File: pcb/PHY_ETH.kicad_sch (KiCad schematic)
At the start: 15 parts, among them U1 LAN8742A, Y1 LFXTAL071758Cutt

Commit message: updated ethernet
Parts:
- added C39: 470pF, Capacitor_SMD:C_0603_1608Metric_Pad1.08x0.95mm_HandSolder, symbol Device:C
- added C40: 1uF, Capacitor_SMD:C_0603_1608Metric_Pad1.08x0.95mm_HandSolder, symbol Device:C
- added C57: 1u, Capacitor_SMD:C_0603_1608Metric, symbol Device:C
- added C58: 1nF, Capacitor_SMD:C_0603_1608Metric_Pad1.08x0.95mm_HandSolder, symbol Device:C
- added C63: 100nF, Capacitor_SMD:C_0603_1608Metric_Pad1.08x0.95mm_HandSolder, symbol Device:C
- added D9: ESDA6V1SC5, Package_TO_SOT_SMD:SOT-23-5, symbol Power_Protection:ESDA6V1SC5
- added FB2: FCM 1608KF-471T03, Inductor_SMD:L_0603_1608Metric_Pad1.05x0.95mm_HandSolder, symbol Device:FerriteBead
- added R27, R28, R41: 10k, Resistor_SMD:R_0603_1608Metric_Pad0.98x0.95mm_HandSolder, symbol Device:R
- added R42, R44, R45: 49.9R, Resistor_SMD:R_0603_1608Metric_Pad0.98x0.95mm_HandSolder, symbol Device:R
- added R50, R51: 75R, Resistor_SMD:R_0603_1608Metric_Pad0.98x0.95mm_HandSolder, symbol Device:R
- added TR1: PT61017PEL, Transformer_SMD:Transformer_Ethernet_Bourns_PT61017PEL, symbol Transformer:PT61017PEL
- C3: value 10uF -> 100nF
- C5, C6: value 10pF -> 8pF
- R10: value 12.4k -> 12.1k
- R8: value 10R -> 49.9R
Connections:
- net 3V3: now also C57.1, FB2.2, R27.1, R28.1, R41.1; no longer R8.1, U1.6 (VDDCR)
- net ETH_CRS_DV: now also R41.2
- net ETH_RXD0: now also R27.2
- net ETH_RXD1: now also R28.2
- net ETH_RXM: now also D9.5 (K), R51.1, TR1.10 (C_RX), TR1.9 (RX-); no longer U1.22 (RXN)
- net ETH_RXP: now also D9.4 (K), TR1.11 (RX+); no longer U1.23 (RXP)
- net ETH_TXM: now also D9.3 (K), TR1.14 (TX-); no longer U1.20 (TXN)
- net ETH_TXP: now also D9.1 (K), TR1.16 (TX+); no longer U1.21 (TXP)
- net GND: now also R9.2, C39.2, C40.2, C57.2, C58.2, C63.2, D9.2 (A); no longer D4.1 (K)
- net at D3.1 (K), R7.2: now also D3.2 (A), U1.2 (LED2/~{INTSEL})
- net at D4.2 (A): now also U1.3 (LED1/REGOFF); no longer R9.2
- net at R9.1: now also D4.1 (K); no longer U1.3 (LED1/REGOFF)
- net at C2.1, C3.1, U1.1 (VDD2A)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: now also R8.1, C63.1, FB2.1, R42.1, R44.1, R45.1, TR1.2 (C_TD), TR1.7 (C_RD); no longer R8.2
- new net: C58.1, R50.2, R51.2
- new net: R42.2, TR1.3 (TD-), U1.20 (TXN)
- new net: R8.2, TR1.1 (TD+), U1.21 (TXP)
- new net: R45.2, TR1.8 (RD-), U1.22 (RXN)
- new net: R44.2, TR1.6 (RD+), U1.23 (RXP)
- new net: C39.1, C40.1, U1.6 (VDDCR)
- new net: R50.1, TR1.15 (C_TX)
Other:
- moved on the sheet: C2, C3, C4, C5, C6, D3, D4, R10, R11, R12, R7, R9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

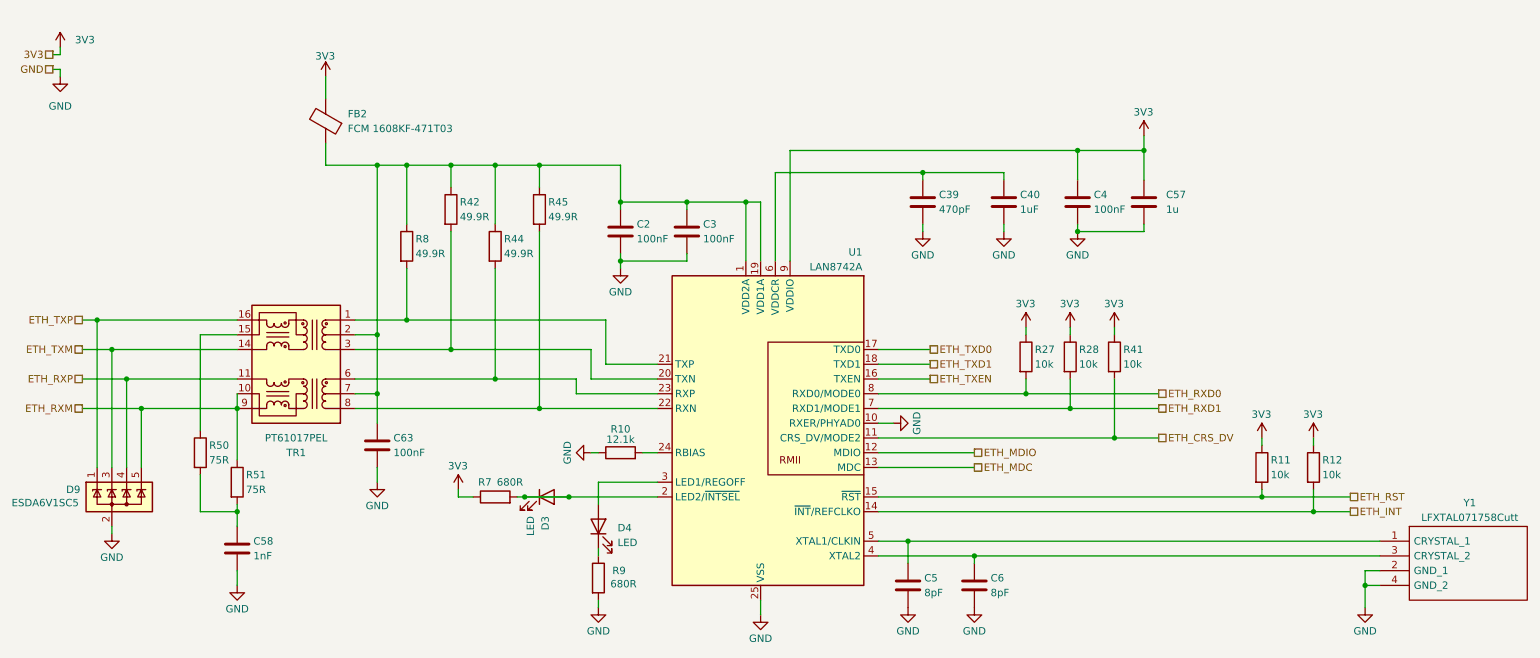
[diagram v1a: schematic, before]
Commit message: reannotated, updated some symbols
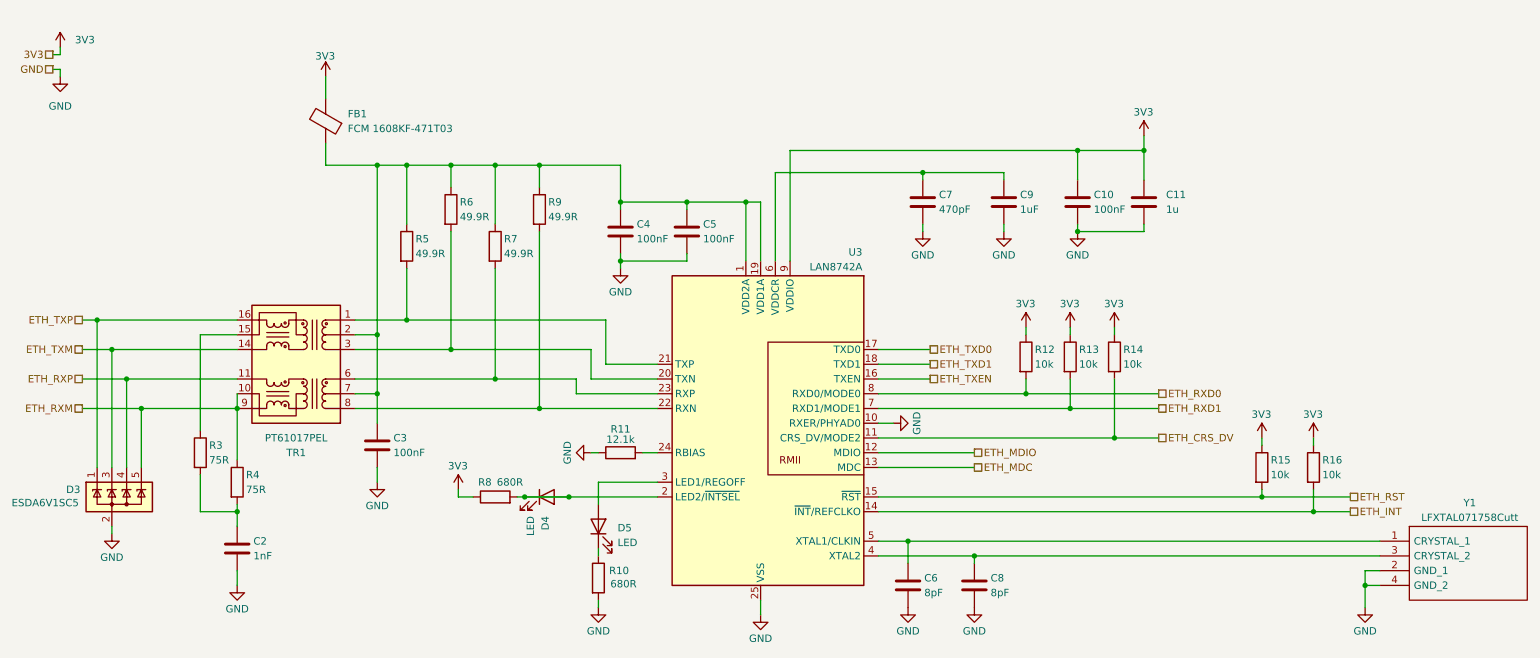
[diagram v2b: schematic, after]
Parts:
- renumbered C4 to C10, C57 to C11, C58 to C2, C63 to C3, C2 to C4, C3 to C5, C5 to C6, C39 to C7, C6 to C8, C40 to C9, D9 to D3, D3 to D4, D4 to D5, FB2 to FB1, R9 to R10, R10 to R11, R27 to R12, R28 to R13, R41 to R14, R11 to R15, R12 to R16, R50 to R3, R51 to R4, R8 to R5, R42 to R6, R44 to R7, R7 to R8, R45 to R9, U1 to U3

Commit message: minor changes before layout
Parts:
- added TP20: ETH_RST, TestPoint:TestPoint_THTPad_D2.0mm_Drill1.0mm, symbol Connector:TestPoint
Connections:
- net ETH_INT: now also R15.2; no longer R16.2
- net ETH_RST: now also R16.2, TP20.1; no longer R15.2
- net at D4.1 (K), R8.2: no longer D4.2 (A), U3.2 (LED2/~{INTSEL})
- new net: D4.2 (A), U3.2 (LED2/~{INTSEL})
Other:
- moved on the sheet: R15, R16
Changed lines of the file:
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@@
 	(paper "A4")
 	(junction
-		(at 114.3 101.6)
-		(diameter 0)
-		(color 0 0 0 0)
-	)
-	(junction
-		(at 233.68 101.6)
+		(at 232.41 104.14)
 		(diameter 0)
 		(color 0 0 0 0)
@@
 	)
 	(junction
-		(at 101.6 44.45)
+		(at 241.3 101.6)
 		(diameter 0)
 		(color 0 0 0 0)
 	)
 	(junction
-		(at 144.78 50.8)
+		(at 101.6 44.45)
 		(diameter 0)
 		(color 0 0 0 0)
 	)
 	(junction
-		(at 106.68 101.6)
+		(at 144.78 50.8)
 		(diameter 0)
 		(color 0 0 0 0)
@@
 	)
 	(junction
-		(at 242.57 104.14)
+		(at 184.15 111.76)
 		(diameter 0)
 		(color 0 0 0 0)
 	)
 	(junction
-		(at 184.15 111.76)
+		(at 57.15 104.14)
 		(diameter 0)
 		(color 0 0 0 0)
 	)
 	(junction
-		(at 57.15 104.14)
+		(at 241.3 90.17)
 		(diameter 0)
 		(color 0 0 0 0)
@@
 	(wire
 		(pts
-			(xy 114.3 101.6) (xy 106.68 101.6)
-		)
-		(stroke
-			(width 0)
-			(type default)
-		)
-	)
-	(wire
-		(pts
 			(xy 184.15 93.98) (xy 167.64 93.98)
 		)
@@
 	(wire
 		(pts
-			(xy 242.57 91.44) (xy 242.57 92.71)
+			(xy 241.3 71.12) (xy 241.3 72.39)
 		)
 		(stroke
@@
 	(wire
 		(pts
-			(xy 167.64 104.14) (xy 242.57 104.14)
+			(xy 167.64 104.14) (xy 232.41 104.14)
 		)
 		(stroke
@@
 	(wire
 		(pts
-			(xy 242.57 104.14) (xy 248.92 104.14)
+			(xy 149.86 45.72) (xy 175.26 45.72)
 		)
 		(stroke
@@
 	(wire
 		(pts
-			(xy 149.86 45.72) (xy 175.26 45.72)
+			(xy 241.3 101.6) (xy 248.92 101.6)
 		)
 		(stroke
@@
 	(wire
 		(pts
-			(xy 233.68 100.33) (xy 233.68 101.6)
-		)
-		(stroke
-			(width 0)
-			(type default)
-		)
-	)
-	(wire
-		(pts
 			(xy 109.22 44.45) (xy 109.22 48.26)
 		)
@@
 	(wire
 		(pts
-			(xy 233.68 101.6) (xy 248.92 101.6)
-		)
-		(stroke
-			(width 0)
-			(type default)
-		)
-	)
-	(wire
-		(pts
 			(xy 95.25 100.33) (xy 95.25 101.6)
 		)
@@
 	(wire
 		(pts
+			(xy 241.3 90.17) (xy 241.3 101.6)
+		)
+		(stroke
+			(width 0)
+			(type default)
+		)
+	)
+	(wire
+		(pts
+			(xy 241.3 90.17) (xy 242.57 90.17)
+		)
+		(stroke
+			(width 0)
+			(type default)
+		)
+	)
+	(wire
+		(pts
 			(xy 213.36 55.88) (xy 213.36 54.61)
 		)
@@
 	(wire
 		(pts
-			(xy 233.68 91.44) (xy 233.68 92.71)
+			(xy 232.41 71.12) (xy 232.41 85.09)
 		)
 		(stroke
@@
 	(wire
 		(pts
-			(xy 167.64 101.6) (xy 233.68 101.6)
+			(xy 167.64 101.6) (xy 241.3 101.6)
 		)
 		(stroke
@@
 	(wire
 		(pts
+			(xy 232.41 92.71) (xy 232.41 104.14)
+		)
+		(stroke
+			(width 0)
+			(type default)
+		)
+	)
+	(wire
+		(pts
 			(xy 175.26 45.72) (xy 189.23 45.72)
 		)
@@
 	(wire
 		(pts
+			(xy 241.3 80.01) (xy 241.3 90.17)
+		)
+		(stroke
+			(width 0)
+			(type default)
+		)
+	)
+	(wire
+		(pts
 			(xy 118.11 81.28) (xy 129.54 81.28)
 		)
@@
 	(wire
 		(pts
-			(xy 81.28 73.66) (xy 81.28 44.45)
+			(xy 232.41 104.14) (xy 248.92 104.14)
 		)
 		(stroke
@@
 	(wire
 		(pts
-			(xy 242.57 100.33) (xy 242.57 104.14)
+			(xy 81.28 73.66) (xy 81.28 44.45)
 		)
 		(stroke
@@
 	(symbol
 		(lib_id "Device:R")
-		(at 242.57 96.52 0)
+		(at 241.3 76.2 0)
 		(unit 1)
 		(exclude_from_sim no)
@@
 		(dnp no)
 		(property "Reference" "R16"
-			(at 244.094 95.25 0)
+			(at 242.824 74.93 0)
 			(effects
 				(font
@@
 		)
 		(property "Value" "10k"
-			(at 244.094 97.79 0)
+			(at 242.824 77.47 0)
 			(effects
 				(font
@@
 		)
 		(property "Footprint" "Resistor_SMD:R_0603_1608Metric_Pad0.98x0.95mm_HandSolder"
-			(at 240.792 96.52 90)
+			(at 239.522 76.2 90)
 			(effects
 				(font
@@
 		)
 		(property "Datasheet" "~"
-			(at 242.57 96.52 0)
+			(at 241.3 76.2 0)
 			(effects
 				(font
@@
 		)
 		(property "Description" "Resistor"
-			(at 242.57 96.52 0)
+			(at 241.3 76.2 0)
 			(effects
 				(font
@@
 	)
 	(symbol
+		(lib_id "Connector:TestPoint")
+		(at 242.57 90.17 270)
+		(unit 1)
+		(exclude_from_sim no)
+		(in_bom yes)
+		(on_board yes)
+		(dnp no)
+		(property "Reference" "TP20"
+			(at 243.332 85.852 90)
+			(effects
+				(font
+					(size 1.27 1.27)
+				)
+				(justify left)
+			)
+		)
+		(property "Value" "ETH_RST"
+			(at 243.332 87.884 90)
+			(effects
+				(font
+					(size 1.27 1.27)
+				)
+				(justify left)
+			)
+		)
+		(property "Footprint" "TestPoint:TestPoint_THTPad_D2.0mm_Drill1.0mm"
+			(at 242.57 95.25 0)
+			(effects
+				(font
+					(size 1.27 1.27)
+				)
+				(hide yes)
+			)
+		)
+		(property "Datasheet" "~"
+			(at 242.57 95.25 0)
+			(effects
+				(font
+					(size 1.27 1.27)
+				)
+				(hide yes)
+			)
+		)
+		(property "Description" "test point"
+			(at 242.57 90.17 0)
+			(effects
+				(font
+					(size 1.27 1.27)
+				)
+				(hide yes)
+			)
+		)
+		(pin "1"
+		)
+		(instances
+			(project "NCU"
+				(path "/3aee14c3-5480-4f7c-989e-3fef81779034/9758cbcc-2ab2-405c-935d-3964f8470771"
+					(reference "TP20")
+					(unit 1)
+				)
+			)
+		)
+	)
+	(symbol
 		(lib_id "power:+3V3")
 		(at 193.04 72.39 0)
@@
 	(symbol
 		(lib_id "Device:R")
-		(at 233.68 96.52 0)
+		(at 232.41 88.9 0)
 		(unit 1)
 		(exclude_from_sim no)
@@
 		(dnp no)
 		(property "Reference" "R15"
-			(at 235.204 95.25 0)
+			(at 233.934 87.63 0)
 			(effects
 				(font
@@
 		)
 		(property "Value" "10k"
-			(at 235.204 97.79 0)
+			(at 233.934 90.17 0)
 			(effects
 				(font
@@
 		)
 		(property "Footprint" "Resistor_SMD:R_0603_1608Metric_Pad0.98x0.95mm_HandSolder"
-			(at 231.902 96.52 90)
+			(at 230.632 88.9 90)
 			(effects
 				(font
@@
 		)
 		(property "Datasheet" "~"
-			(at 233.68 96.52 0)
+			(at 232.41 88.9 0)
 			(effects
 				(font
@@
 		)
 		(property "Description" "Resistor"
-			(at 233.68 96.52 0)
+			(at 232.41 88.9 0)
 			(effects
 				(font
@@
 	(symbol
 		(lib_id "power:+3V3")
-		(at 233.68 91.44 0)
+		(at 232.41 71.12 0)
 		(unit 1)
 		(exclude_from_sim no)
@@
 		(dnp no)
 		(property "Reference" "#PWR0114"
-			(at 233.68 95.25 0)
+			(at 232.41 74.93 0)
 			(effects
 				(font
@@
 		)
 		(property "Value" "3V3"
-			(at 231.902 87.376 0)
+			(at 230.632 67.056 0)
 			(effects
 				(font
@@
 		)
 		(property "Footprint" ""
-			(at 233.68 91.44 0)
+			(at 232.41 71.12 0)
 			(effects
 				(font
@@
 		)
 		(property "Datasheet" ""
-			(at 233.68 91.44 0)
+			(at 232.41 71.12 0)
 			(effects
 				(font
@@
 		)
 		(property "Description" "Power symbol creates a global label with name \"+3V3\""
-			(at 233.68 91.44 0)
+			(at 232.41 71.12 0)
 			(effects
 				(font
@@
 	(symbol
 		(lib_id "power:+3V3")
-		(at 242.57 91.44 0)
+		(at 241.3 71.12 0)
 		(unit 1)
 		(exclude_from_sim no)
@@
 		(dnp no)
 		(property "Reference" "#PWR0115"
-			(at 242.57 95.25 0)
+			(at 241.3 74.93 0)
 			(effects
 				(font
@@
 		)
 		(property "Value" "3V3"
-			(at 240.792 87.376 0)
+			(at 239.522 67.056 0)
 			(effects
 				(font
@@
 		)
 		(property "Footprint" ""
-			(at 242.57 91.44 0)
+			(at 241.3 71.12 0)
 			(effects
 				(font
@@
 		)
 		(property "Datasheet" ""
-			(at 242.57 91.44 0)
+			(at 241.3 71.12 0)
 			(effects
 				(font
@@
 		)
 		(property "Description" "Power symbol creates a global label with name \"+3V3\""
-			(at 242.57 91.44 0)
+			(at 241.3 71.12 0)
 			(effects
 				(font

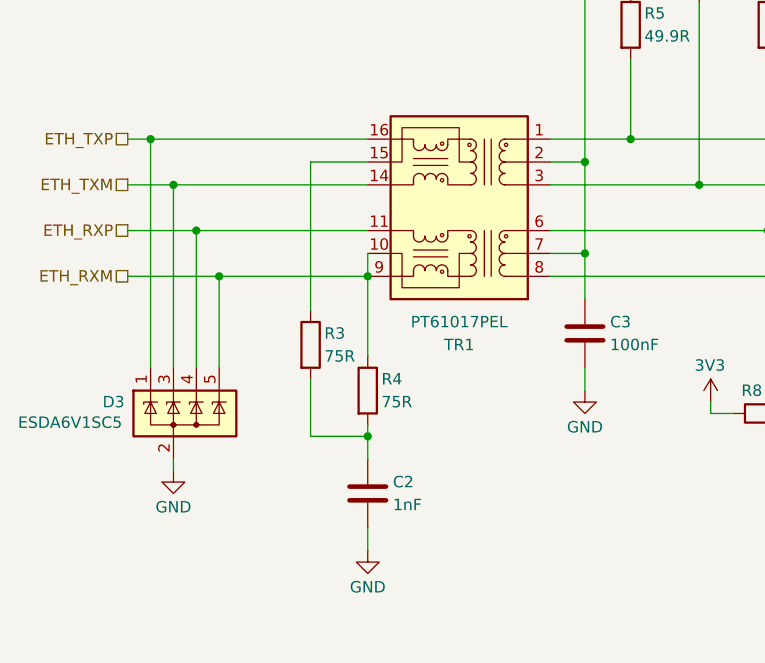
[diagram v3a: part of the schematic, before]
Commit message: first pass of ethernet phy
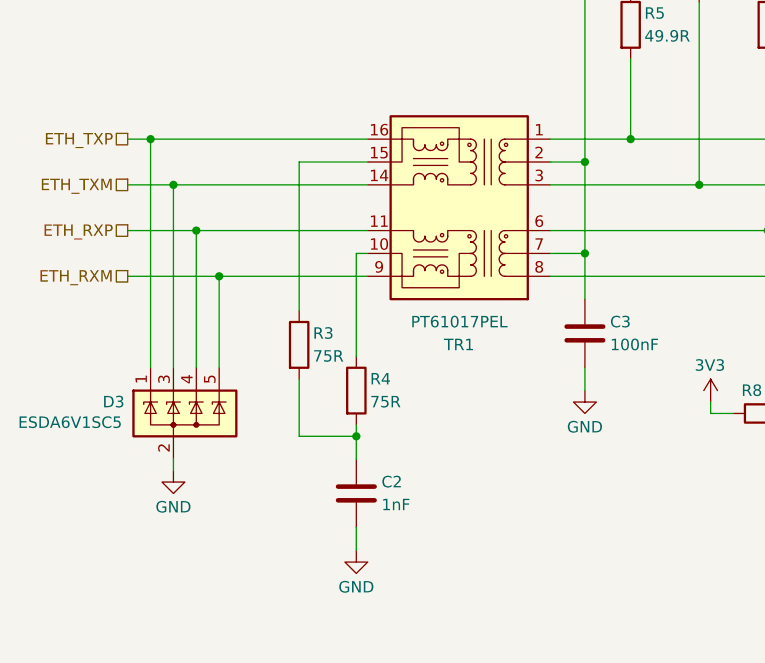
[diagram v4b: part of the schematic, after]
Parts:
- C11: footprint Capacitor_SMD:C_0603_1608Metric -> Capacitor_SMD:C_0603_1608Metric_Pad1.08x0.95mm_HandSolder
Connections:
- net ETH_RXM: no longer R4.1, TR1.10 (C_RX)
- new net: R4.1, TR1.10 (C_RX)
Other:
- moved on the sheet: C2, R3, R4
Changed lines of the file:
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@@
 	)
 	(junction
-		(at 57.15 86.36)
-		(diameter 0)
-		(color 0 0 0 0)
-	)
-	(junction
 		(at 86.36 44.45)
 		(diameter 0)
@@
 	)
 	(junction
-		(at 57.15 104.14)
+		(at 55.88 104.14)
 		(diameter 0)
 		(color 0 0 0 0)
@@
 	(wire
 		(pts
-			(xy 57.15 86.36) (xy 57.15 83.82)
-		)
-		(stroke
-			(width 0)
-			(type default)
-		)
-	)
-	(wire
-		(pts
 			(xy 109.22 86.36) (xy 129.54 86.36)
 		)
@@
 	(wire
 		(pts
-			(xy 50.8 104.14) (xy 57.15 104.14)
+			(xy 49.53 104.14) (xy 55.88 104.14)
 		)
 		(stroke
@@
 	(wire
 		(pts
-			(xy 50.8 90.17) (xy 50.8 73.66)
+			(xy 49.53 90.17) (xy 49.53 73.66)
+		)
+		(stroke
+			(width 0)
+			(type default)
+		)
+	)
+	(wire
+		(pts
+			(xy 55.88 95.25) (xy 55.88 83.82)
 		)
 		(stroke
@@
 	(wire
 		(pts
-			(xy 50.8 97.79) (xy 50.8 104.14)
+			(xy 49.53 97.79) (xy 49.53 104.14)
 		)
 		(stroke
@@
 	(wire
 		(pts
-			(xy 50.8 73.66) (xy 57.15 73.66)
+			(xy 49.53 73.66) (xy 57.15 73.66)
 		)
 		(stroke
@@
 	(wire
 		(pts
-			(xy 57.15 104.14) (xy 57.15 106.68)
+			(xy 55.88 104.14) (xy 55.88 106.68)
 		)
 		(stroke
@@
 	(wire
 		(pts
-			(xy 57.15 114.3) (xy 57.15 116.84)
+			(xy 55.88 114.3) (xy 55.88 116.84)
 		)
 		(stroke
@@
 	(wire
 		(pts
-			(xy 57.15 104.14) (xy 57.15 102.87)
+			(xy 55.88 104.14) (xy 55.88 102.87)
 		)
 		(stroke
@@
 	(wire
 		(pts
-			(xy 57.15 95.25) (xy 57.15 86.36)
+			(xy 72.39 40.64) (xy 72.39 44.45)
 		)
 		(stroke
@@
 	(wire
 		(pts
-			(xy 72.39 40.64) (xy 72.39 44.45)
+			(xy 251.46 116.84) (xy 251.46 120.65)
 		)
 		(stroke
@@
 	(wire
 		(pts
-			(xy 251.46 116.84) (xy 251.46 120.65)
+			(xy 251.46 114.3) (xy 251.46 116.84)
 		)
 		(stroke
@@
 	(wire
 		(pts
-			(xy 251.46 114.3) (xy 251.46 116.84)
+			(xy 119.38 99.06) (xy 119.38 102.87)
 		)
 		(stroke
@@
 	(wire
 		(pts
-			(xy 119.38 99.06) (xy 119.38 102.87)
+			(xy 105.41 101.6) (xy 106.68 101.6)
 		)
 		(stroke
@@
 	(wire
 		(pts
-			(xy 105.41 101.6) (xy 106.68 101.6)
+			(xy 172.72 109.22) (xy 172.72 113.03)
 		)
 		(stroke
@@
 	(wire
 		(pts
-			(xy 172.72 109.22) (xy 172.72 113.03)
+			(xy 55.88 83.82) (xy 57.15 83.82)
 		)
 		(stroke
@@
 	(symbol
 		(lib_id "Device:C")
-		(at 57.15 110.49 0)
+		(at 55.88 110.49 0)
 		(unit 1)
 		(exclude_from_sim no)
@@
 		(dnp no)
 		(property "Reference" "C2"
-			(at 59.944 109.22 0)
+			(at 58.674 109.22 0)
 			(effects
 				(font
@@
 		)
 		(property "Value" "1nF"
-			(at 59.944 111.76 0)
+			(at 58.674 111.76 0)
 			(effects
 				(font
@@
 		)
 		(property "Footprint" "Capacitor_SMD:C_0603_1608Metric_Pad1.08x0.95mm_HandSolder"
-			(at 58.1152 114.3 0)
+			(at 56.8452 114.3 0)
 			(effects
 				(font
@@
 		)
 		(property "Datasheet" "~"
-			(at 57.15 110.49 0)
+			(at 55.88 110.49 0)
 			(effects
 				(font
@@
 		)
 		(property "Description" "Unpolarized capacitor"
-			(at 57.15 110.49 0)
+			(at 55.88 110.49 0)
 			(effects
 				(font
@@
 			)
 		)
-		(property "Footprint" "Capacitor_SMD:C_0603_1608Metric"
+		(property "Footprint" "Capacitor_SMD:C_0603_1608Metric_Pad1.08x0.95mm_HandSolder"
 			(at 214.3252 54.61 0)
 			(effects
@@
 	(symbol
 		(lib_id "Device:R")
-		(at 50.8 93.98 0)
+		(at 49.53 93.98 0)
 		(unit 1)
 		(exclude_from_sim no)
@@
 		(dnp no)
 		(property "Reference" "R3"
-			(at 52.324 92.71 0)
+			(at 51.054 92.71 0)
 			(effects
 				(font
@@
 		)
 		(property "Value" "75R"
-			(at 52.324 95.25 0)
+			(at 51.054 95.25 0)
 			(effects
 				(font
@@
 		)
 		(property "Footprint" "Resistor_SMD:R_0603_1608Metric_Pad0.98x0.95mm_HandSolder"
-			(at 49.022 93.98 90)
+			(at 47.752 93.98 90)
 			(effects
 				(font
@@
 		)
 		(property "Datasheet" "~"
-			(at 50.8 93.98 0)
+			(at 49.53 93.98 0)
 			(effects
 				(font
@@
 		)
 		(property "Description" "Resistor"
-			(at 50.8 93.98 0)
+			(at 49.53 93.98 0)
 			(effects
 				(font
@@
 	(symbol
 		(lib_id "Device:R")
-		(at 57.15 99.06 0)
+		(at 55.88 99.06 0)
 		(unit 1)
 		(exclude_from_sim no)
@@
 		(dnp no)
 		(property "Reference" "R4"
-			(at 58.674 97.79 0)
+			(at 57.404 97.79 0)
 			(effects
 				(font
@@
 		)
 		(property "Value" "75R"
-			(at 58.674 100.33 0)
+			(at 57.404 100.33 0)
 			(effects
 				(font
@@
 		)
 		(property "Footprint" "Resistor_SMD:R_0603_1608Metric_Pad0.98x0.95mm_HandSolder"
-			(at 55.372 99.06 90)
+			(at 54.102 99.06 90)
 			(effects
 				(font
@@
 		)
 		(property "Datasheet" "~"
-			(at 57.15 99.06 0)
+			(at 55.88 99.06 0)
 			(effects
 				(font
@@
 		)
 		(property "Description" "Resistor"
-			(at 57.15 99.06 0)
+			(at 55.88 99.06 0)
 			(effects
 				(font
@@
 	(symbol
 		(lib_id "power:GND")
-		(at 57.15 116.84 0)
+		(at 55.88 116.84 0)
 		(mirror y)
 		(unit 1)
@@
 		(dnp no)
 		(property "Reference" "#PWR096"
-			(at 57.15 123.19 0)
+			(at 55.88 123.19 0)
 			(effects
 				(font
@@
 		)
 		(property "Value" "GND"
-			(at 57.15 120.904 0)
+			(at 55.88 120.904 0)
 			(effects
 				(font
@@
 		)
 		(property "Footprint" ""
-			(at 57.15 116.84 0)
+			(at 55.88 116.84 0)
 			(effects
 				(font
@@
 		)
 		(property "Datasheet" ""
-			(at 57.15 116.84 0)
+			(at 55.88 116.84 0)
 			(effects
 				(font
@@
 		)
 		(property "Description" "Power symbol creates a global label with name \"GND\" , ground"
-			(at 57.15 116.84 0)
+			(at 55.88 116.84 0)
 			(effects
 				(font
